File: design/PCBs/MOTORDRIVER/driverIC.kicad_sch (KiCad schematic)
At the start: 8 parts, among them U1 TMC4671-LA

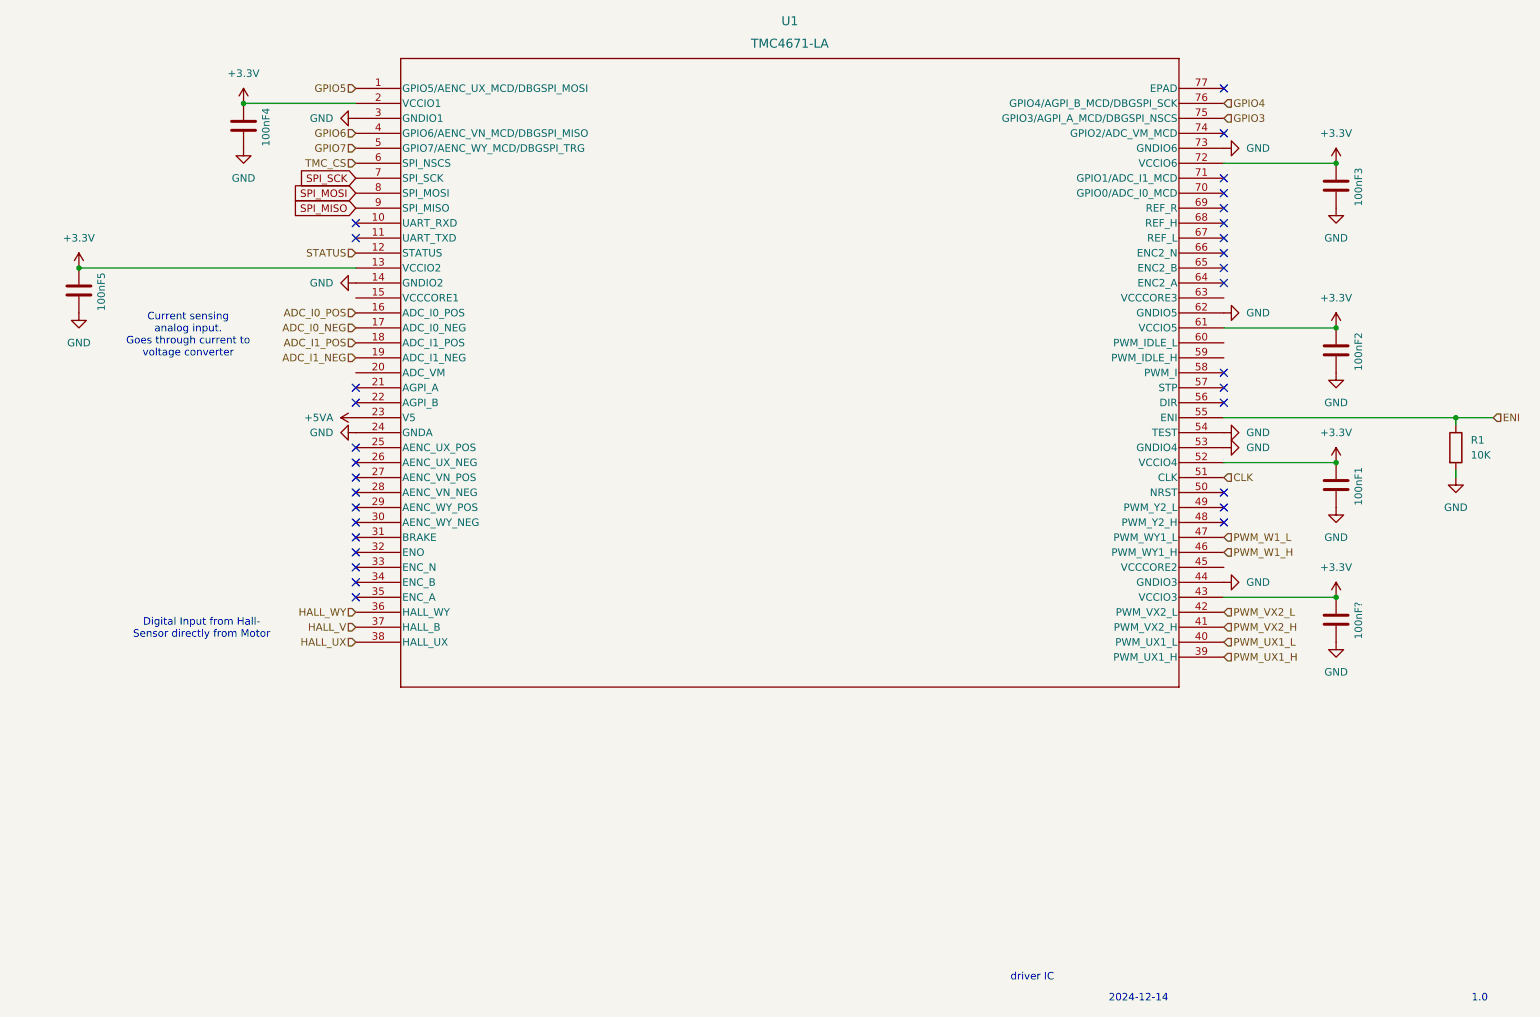
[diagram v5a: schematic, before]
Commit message: cleaned up, added values and footprints
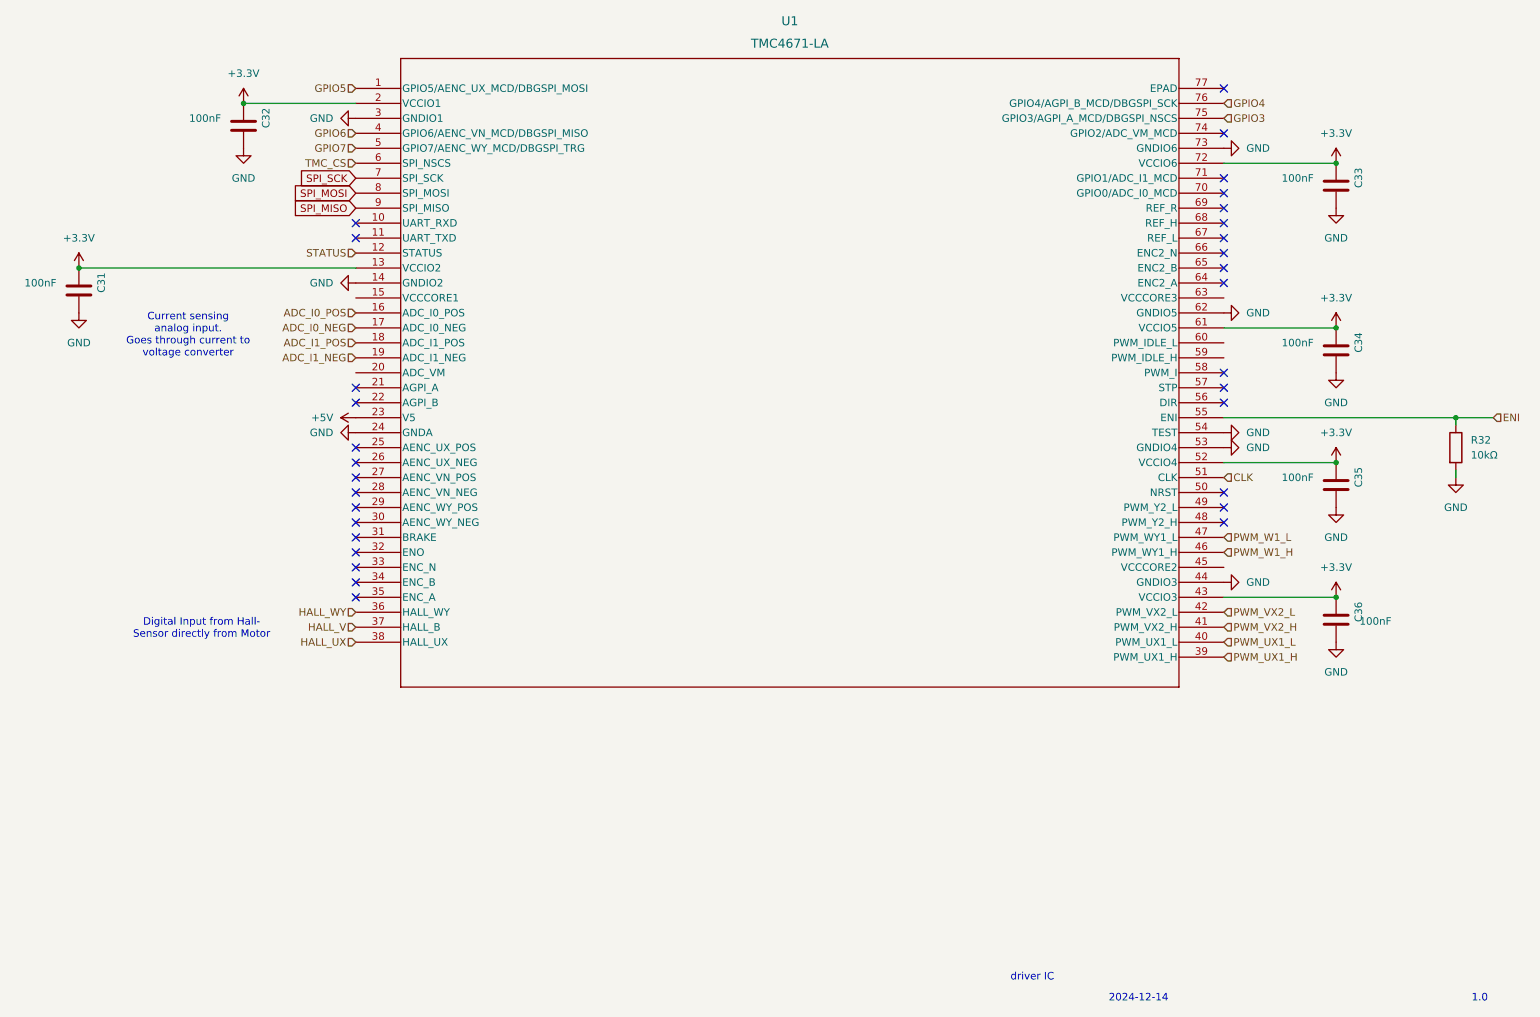
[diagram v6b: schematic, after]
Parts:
- C31: renamed from 100nF5; value C -> 100nF; footprint (none) -> Capacitor_SMD:C_0603_1608Metric
- C32: renamed from 100nF4; value C -> 100nF; footprint (none) -> Capacitor_SMD:C_0603_1608Metric
- C33: renamed from 100nF3; value C -> 100nF; footprint (none) -> Capacitor_SMD:C_0603_1608Metric
- C34: renamed from 100nF2; value C -> 100nF; footprint (none) -> Capacitor_SMD:C_0603_1608Metric
- C35: renamed from 100nF1; value C -> 100nF; footprint (none) -> Capacitor_SMD:C_0603_1608Metric
- C36: renamed from 100nF?; value C -> 100nF; footprint (none) -> Capacitor_SMD:C_0603_1608Metric
- R32: renamed from R1; value 10K -> 10kΩ; footprint (none) -> Resistor_SMD:R_0603_1608Metric
- U1: footprint QFN76_10P5X6P5_TRI -> Custom_Motor_Driver:QFN76_10P5X6P5_TRI
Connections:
- net +5VA renamed +5V

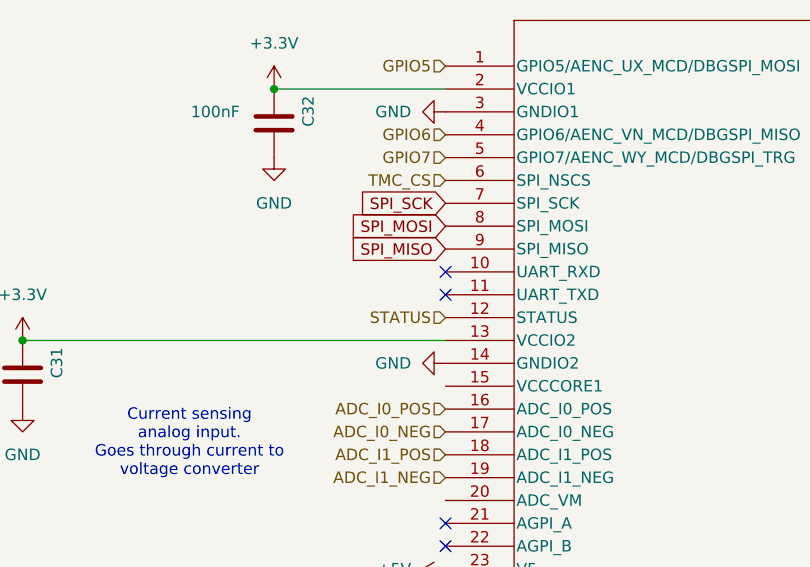
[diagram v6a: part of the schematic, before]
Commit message: uart for tmc-mcu comms
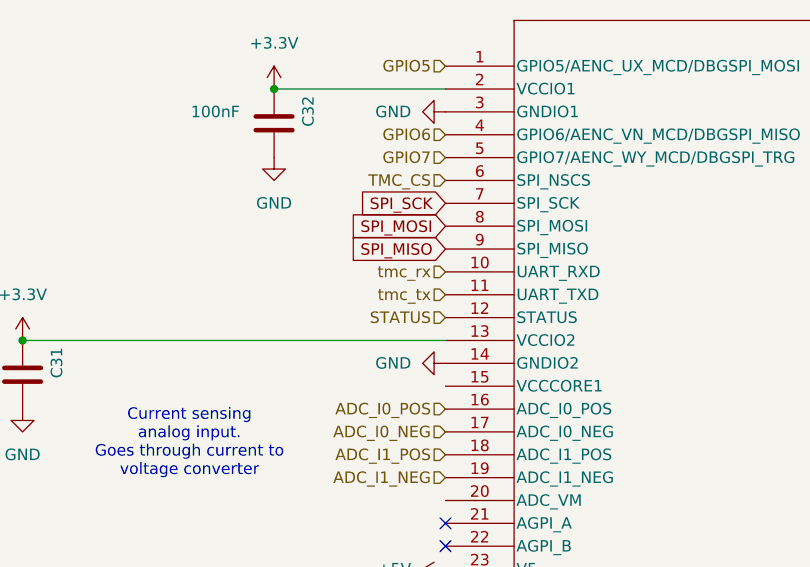
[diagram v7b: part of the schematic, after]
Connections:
- net tmc_rx: now reaches U1.10 (UART_RXD)
- net tmc_tx: now reaches U1.11 (UART_TXD)
- no-connect marks 31 -> 29
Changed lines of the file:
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@@
-	)
-	(no_connect
-		(at 80.01 64.77)
 	)
 	(no_connect
@@
 	(no_connect
 		(at 227.33 59.69)
-	)
-	(no_connect
-		(at 80.01 62.23)
 	)
 	(no_connect
@@
 		)
 	)
+	(hierarchical_label "tmc_tx"
+		(shape input)
+		(at 80.01 64.77 180)
+		(fields_autoplaced yes)
+		(effects
+			(font
+				(size 1.27 1.27)
+			)
+			(justify right)
+		)
+	)
 	(hierarchical_label "GPIO5"
 		(shape input)
@@
 		(fields_autoplaced yes)
 		(effects
+			(font
+				(size 1.27 1.27)
+			)
+			(justify right)
+		)
+	)
+	(hierarchical_label "tmc_rx"
+		(shape input)
+		(at 80.01 62.23 180)
+		(fields_autoplaced yes)
+		(effects

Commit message: fixed references
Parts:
- renumbered U1 to U4
